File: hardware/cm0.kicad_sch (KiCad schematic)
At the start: 0 parts

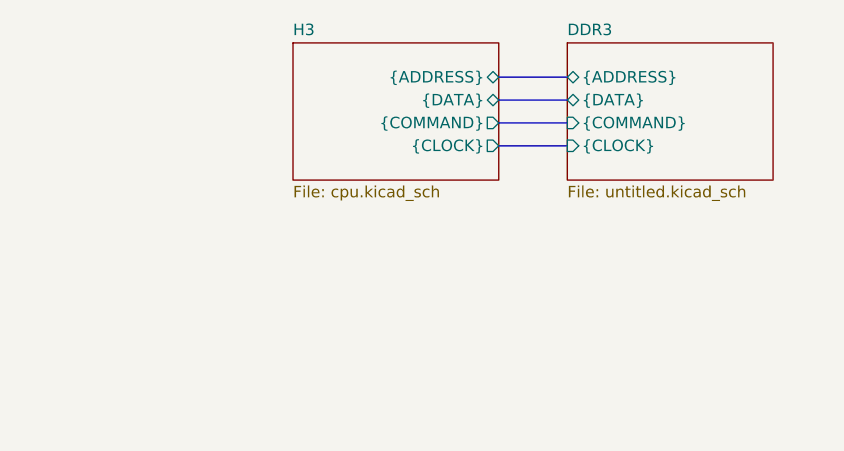
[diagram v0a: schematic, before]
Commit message: Drew wifi, GPDI, and re-routed DDR3
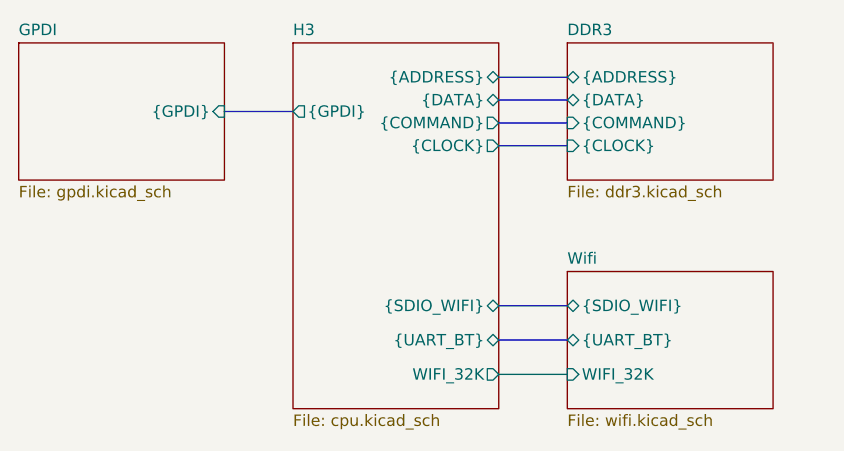
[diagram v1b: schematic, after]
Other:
- added sheet GPDI (gpdi.kicad_sch)
- added sheet Wifi (wifi.kicad_sch)
- sheet DDR3: file untitled.kicad_sch -> ddr3.kicad_sch
- sheet H3 ports: added WIFI_32K, {GPDI}, {SDIO_WIFI}, {UART_BT}; removed none
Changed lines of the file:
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@@
+	(bus
+		(pts
+			(xy 93.98 40.64) (xy 101.6 40.64)
+		)
+		(stroke
+			(width 0)
+			(type default)
+		)
+	)
+	(bus
+		(pts
+			(xy 124.46 62.23) (xy 132.08 62.23)
+		)
+		(stroke
+			(width 0)
+			(type default)
+		)
+	)
+	(wire
+		(pts
+			(xy 124.46 69.85) (xy 132.08 69.85)
+		)
+		(stroke
+			(width 0)
+			(type default)
+		)
+	)
+	(bus
+		(pts
+			(xy 124.46 66.04) (xy 132.08 66.04)
+		)
+		(stroke
+			(width 0)
+			(type default)
+		)
+	)
 	(bus
 		(pts
@@
 			)
 		)
-		(property "Sheetfile" "untitled.kicad_sch"
+		(property "Sheetfile" "ddr3.kicad_sch"
 			(at 132.08 48.8446 0)
 			(effects
@@
 	)
 	(sheet
-		(at 101.6 33.02)
+		(at 132.08 58.42)
 		(size 22.86 15.24)
 		(exclude_from_sim no)
@@
 			(color 0 0 0 0.0000)
 		)
+		(property "Sheetname" "Wifi"
+			(at 132.08 57.7084 0)
+			(effects
+				(font
+					(size 1.27 1.27)
+				)
+				(justify left bottom)
+			)
+		)
+		(property "Sheetfile" "wifi.kicad_sch"
+			(at 132.08 74.2446 0)
+			(effects
+				(font
+					(size 1.27 1.27)
+				)
+				(justify left top)
+			)
+		)
+		(pin "WIFI_32K" input
+			(at 132.08 69.85 180)
+			(effects
+				(font
+					(size 1.27 1.27)
+				)
+				(justify left)
+			)
+		)
+		(pin "{SDIO_WIFI}" bidirectional
+			(at 132.08 62.23 180)
+			(effects
+				(font
+					(size 1.27 1.27)
+				)
+				(justify left)
+			)
+		)
+		(pin "{UART_BT}" bidirectional
+			(at 132.08 66.04 180)
+			(effects
+				(font
+					(size 1.27 1.27)
+				)
+				(justify left)
+			)
+		)
+		(instances
+			(project "cm0"
+				(path "/b53f5dbb-8078-4818-9e8f-fdf90ba6d854"
+					(page "4")
+				)
+			)
+		)
+	)
+	(sheet
+		(at 71.12 33.02)
+		(size 22.86 15.24)
+		(exclude_from_sim no)
+		(in_bom yes)
+		(on_board yes)
+		(dnp no)
+		(fields_autoplaced yes)
+		(stroke
+			(width 0.1524)
+			(type solid)
+		)
+		(fill
+			(color 0 0 0 0.0000)
+		)
+		(property "Sheetname" "GPDI"
+			(at 71.12 32.3084 0)
+			(effects
+				(font
+					(size 1.27 1.27)
+				)
+				(justify left bottom)
+			)
+		)
+		(property "Sheetfile" "gpdi.kicad_sch"
+			(at 71.12 48.8446 0)
+			(effects
+				(font
+					(size 1.27 1.27)
+				)
+				(justify left top)
+			)
+		)
+		(pin "{GPDI}" input
+			(at 93.98 40.64 0)
+			(effects
+				(font
+					(size 1.27 1.27)
+				)
+				(justify right)
+			)
+		)
+		(instances
+			(project "cm0"
+				(path "/b53f5dbb-8078-4818-9e8f-fdf90ba6d854"
+					(page "5")
+				)
+			)
+		)
+	)
+	(sheet
+		(at 101.6 33.02)
+		(size 22.86 40.64)
+		(exclude_from_sim no)
+		(in_bom yes)
+		(on_board yes)
+		(dnp no)
+		(fields_autoplaced yes)
+		(stroke
+			(width 0.1524)
+			(type solid)
+		)
+		(fill
+			(color 0 0 0 0.0000)
+		)
 		(property "Sheetname" "H3"
 			(at 101.6 32.3084 0)
@@
 		)
 		(property "Sheetfile" "cpu.kicad_sch"
-			(at 101.6 48.8446 0)
+			(at 101.6 74.2446 0)
 			(effects
 				(font
@@
 			)
 		)
+		(pin "{SDIO_WIFI}" bidirectional
+			(at 124.46 62.23 0)
+			(effects
+				(font
+					(size 1.27 1.27)
+				)
+				(justify right)
+			)
+		)
+		(pin "{UART_BT}" bidirectional
+			(at 124.46 66.04 0)
+			(effects
+				(font
+					(size 1.27 1.27)
+				)
+				(justify right)
+			)
+		)
+		(pin "WIFI_32K" output
+			(at 124.46 69.85 0)
+			(effects
+				(font
+					(size 1.27 1.27)
+				)
+				(justify right)
+			)
+		)
+		(pin "{GPDI}" output
+			(at 101.6 40.64 180)
+			(effects
+				(font
+					(size 1.27 1.27)
+				)
+				(justify left)
+			)
+		)
